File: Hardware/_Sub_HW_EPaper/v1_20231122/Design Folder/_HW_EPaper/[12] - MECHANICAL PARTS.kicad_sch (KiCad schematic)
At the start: 0 parts

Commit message: Latest update
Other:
- company: (none) -> Mend0z0
- title: (none) -> _HW_EPaper
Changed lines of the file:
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@@
 (kicad_sch (version 20230121) (generator eeschema)
   (paper "B")
+  (title_block
+    (title "_HW_EPaper")
+    (rev "v1.0")
+    (company "Mend0z0")
+    (comment 1 "v1.0")
+    (comment 2 "PRELIMINARY")
+  )
   (text "LI-ION BATTERY 1cell 3.7v" (at 71.12 63.5 0)
     (effects (font (size 5.08 5.08)) (justify left bottom))

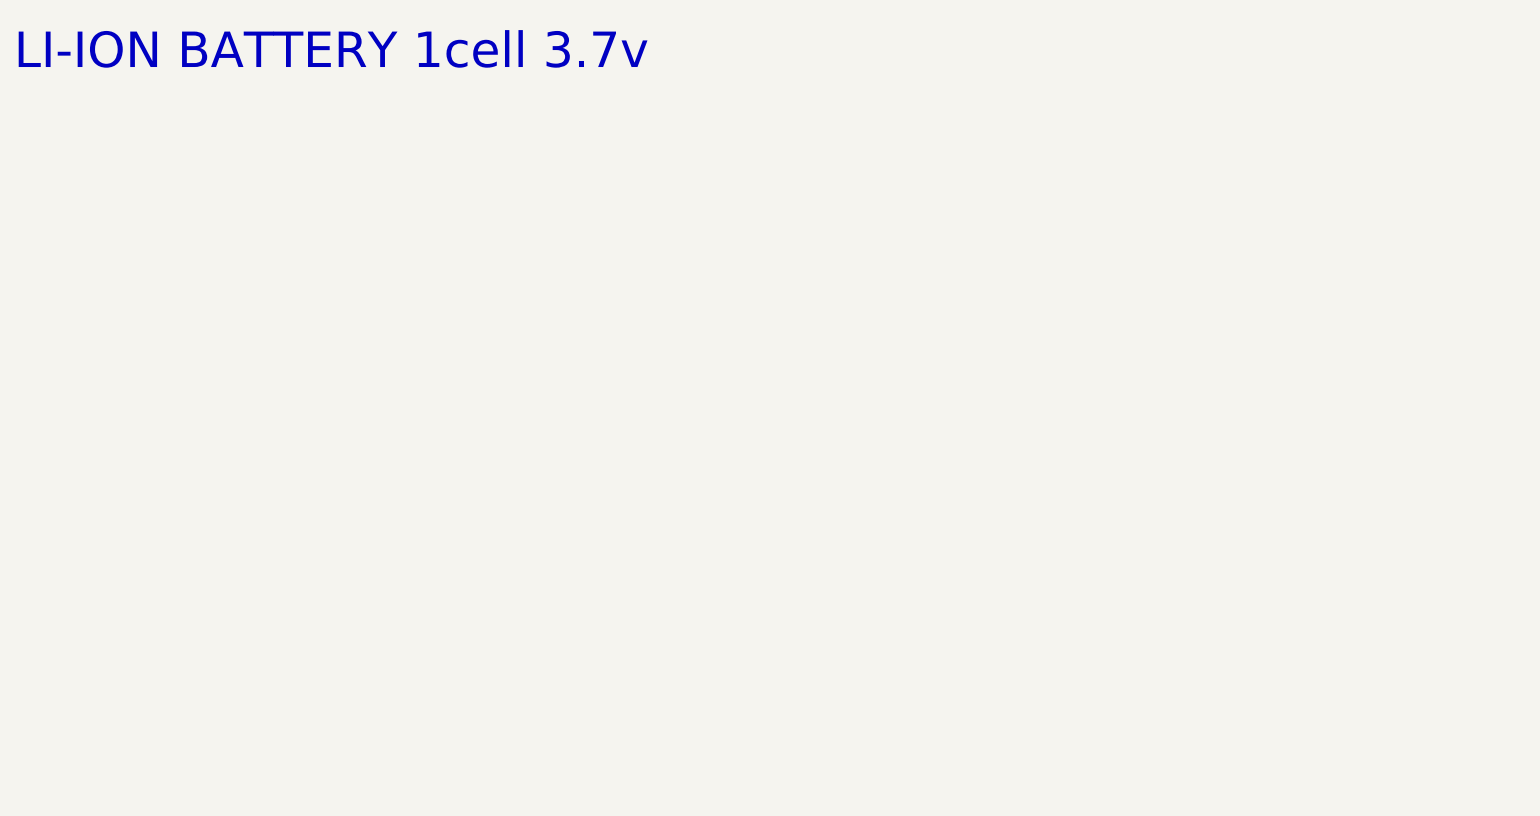
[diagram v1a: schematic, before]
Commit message: Working on epaper hardware
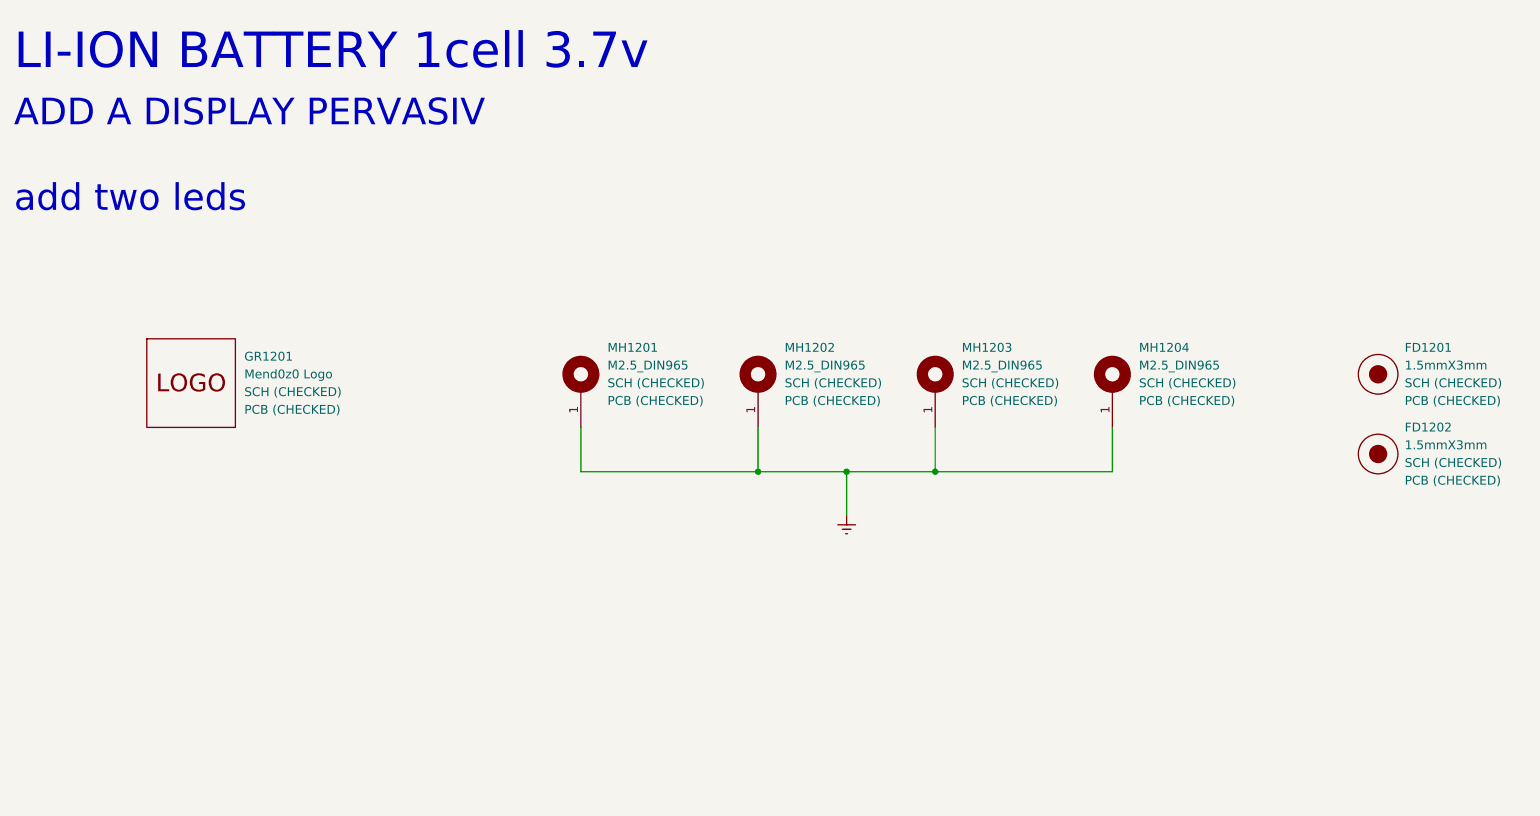
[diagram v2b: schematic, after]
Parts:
- added FD1201, FD1202: 1.5mmX3mm, Fiducial:Fiducial_1.5mm_Mask3mm, symbol _SCHLIB_Epaper:MECH_PAD_FIDUCIAL_1.5mm_3mm
- added GR1201: Mend0z0 Logo, _PCBLIB_Epaper:LOGO_MEND0Z0, symbol _SCHLIB_Epaper:MECH_GR_LOGO_MEND0Z0_TOP LAYER
- added MH1201, MH1202, MH1203, MH1204: M2.5_DIN965, MountingHole:MountingHole_2.7mm_M2.5_DIN965_Pad, symbol _SCHLIB_Epaper:MECH_HOLE_MOUNTING_M2.5_DIN965_WITH NET
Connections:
- new net Earth: MH1201.1, MH1202.1, MH1203.1, MH1204.1
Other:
- note added: "ADD A DISPLAY PERVASIV add two leds"

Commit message: Updating file templates and structures...
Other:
- note added: "ADD A DISPLAY PERVASIV add two leds THD ADD a BOX and screws"
- note removed: "ADD A DISPLAY PERVASIV add two leds"
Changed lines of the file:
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@@
 (kicad_sch (version 20230121) (generator eeschema)
-  (paper "B")
+  (paper "C")
   (title_block
     (title "_HW_EPaper")
@@
     (stroke (width 0) (type default))
   )
-  (text "ADD A DISPLAY PERVASIV\n\nadd two leds" (at 71.12 83.82 0)
+  (text "ADD A DISPLAY PERVASIV\n\nadd two leds THD\n\nADD a BOX and screws"
+    (at 77.47 166.37 0)
     (effects (font (size 3.81 3.81)) (justify left bottom))
   )
-  (text "LI-ION BATTERY 1cell 3.7v" (at 71.12 63.5 0)
+  (text "LI-ION BATTERY 1cell 3.7v" (at 76.2 130.81 0)
     (effects (font (size 5.08 5.08)) (justify left bottom))
   )
@@
       (effects (font (size 1.27 1.27)) (justify left) hide)
     )
-    (property "Part Number" "" (at 92.71 82.55 0)
-      (effects (font (size 1.27 1.27)) (justify left) hide)
-    )
-    (property "Link" "" (at 92.71 90.17 0)
-      (effects (font (size 1.27 1.27)) (justify left) hide)
-    )
-    (property "Package" "" (at 92.71 80.01 0)
-      (effects (font (size 1.27 1.27)) (justify left))
-    )
     (property "SCH CHECK" "SCH (CHECKED)" (at 104.14 109.22 0)
       (effects (font (size 1.27 1.27)) (justify left))
@@
       (effects (font (size 1.27 1.27)) (justify left) hide)
     )
-    (property "Part Number" "" (at 184.15 111.76 0)
-      (effects (font (size 1.27 1.27)) (justify left) hide)
-    )
-    (property "Link" "" (at 191.77 111.76 0)
-      (effects (font (size 1.27 1.27)) (justify left) hide)
-    )
-    (property "Package" "" (at 181.61 111.76 0)
-      (effects (font (size 1.27 1.27)) (justify left))
-    )
     (property "SCH CHECK" "SCH (CHECKED)" (at 207.01 107.95 90)
       (effects (font (size 1.27 1.27)) (justify right))
@@
     (property "Description" "Mounting Hole, M2.5 (DIN965 Standard), with net" (at 163.83 111.76 0)
       (effects (font (size 1.27 1.27)) (justify left) hide)
-    )
-    (property "Part Number" "" (at 158.75 111.76 0)
-      (effects (font (size 1.27 1.27)) (justify left) hide)
-    )
-    (property "Link" "" (at 166.37 111.76 0)
-      (effects (font (size 1.27 1.27)) (justify left) hide)
-    )
-    (property "Package" "" (at 156.21 111.76 0)
-      (effects (font (size 1.27 1.27)) (justify left))
     )
     (property "SCH CHECK" "SCH (CHECKED)" (at 181.61 107.95 90)
@@
       (effects (font (size 1.27 1.27)) (justify left) hide)
     )
-    (property "Part Number" "" (at 266.7 85.09 0)
-      (effects (font (size 1.27 1.27)) (justify left) hide)
-    )
-    (property "Link" "" (at 266.7 92.71 0)
-      (effects (font (size 1.27 1.27)) (justify left) hide)
-    )
-    (property "Package" "" (at 266.7 82.55 0)
-      (effects (font (size 1.27 1.27)) (justify left))
-    )
     (property "SCH CHECK" "SCH (CHECKED)" (at 270.51 107.95 0)
       (effects (font (size 1.27 1.27)) (justify left))
@@
       (effects (font (size 1.27 1.27)) (justify left) hide)
     )
-    (property "Part Number" "" (at 209.55 111.76 0)
-      (effects (font (size 1.27 1.27)) (justify left) hide)
-    )
-    (property "Link" "" (at 217.17 111.76 0)
-      (effects (font (size 1.27 1.27)) (justify left) hide)
-    )
-    (property "Package" "" (at 207.01 111.76 0)
-      (effects (font (size 1.27 1.27)) (justify left))
-    )
     (property "SCH CHECK" "SCH (CHECKED)" (at 232.41 107.95 90)
       (effects (font (size 1.27 1.27)) (justify right))
@@
       (effects (font (size 1.27 1.27)) (justify left) hide)
     )
-    (property "Part Number" "" (at 133.35 111.76 0)
-      (effects (font (size 1.27 1.27)) (justify left) hide)
-    )
-    (property "Link" "" (at 140.97 111.76 0)
-      (effects (font (size 1.27 1.27)) (justify left) hide)
-    )
-    (property "Package" "" (at 130.81 111.76 0)
-      (effects (font (size 1.27 1.27)) (justify left))
-    )
     (property "SCH CHECK" "SCH (CHECKED)" (at 156.21 107.95 90)
       (effects (font (size 1.27 1.27)) (justify right))
@@
       (effects (font (size 1.27 1.27)) (justify left) hide)
     )
-    (property "Part Number" "" (at 266.7 96.52 0)
-      (effects (font (size 1.27 1.27)) (justify left) hide)
-    )
-    (property "Link" "" (at 266.7 104.14 0)
-      (effects (font (size 1.27 1.27)) (justify left) hide)
-    )
-    (property "Package" "" (at 266.7 93.98 0)
-      (effects (font (size 1.27 1.27)) (justify left))
-    )
     (property "SCH CHECK" "SCH (CHECKED)" (at 270.51 119.38 0)
